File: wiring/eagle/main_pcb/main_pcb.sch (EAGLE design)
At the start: 19 parts

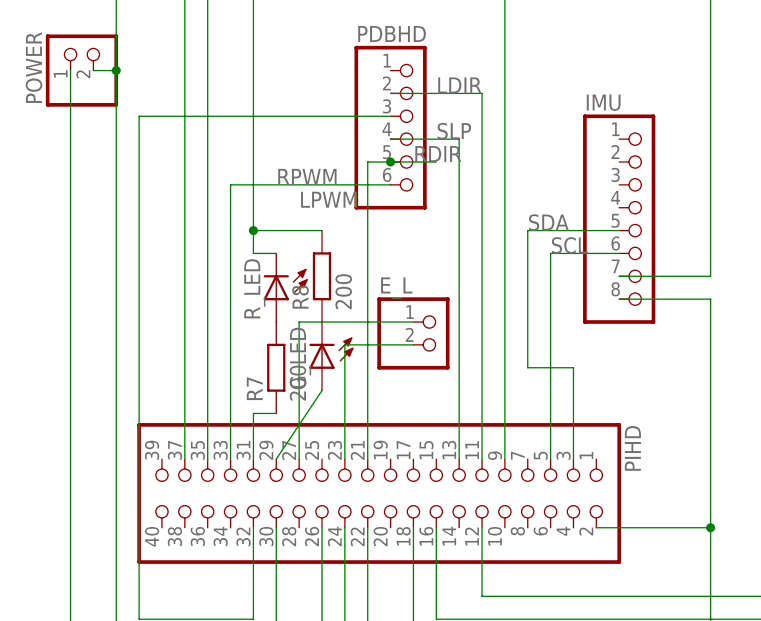
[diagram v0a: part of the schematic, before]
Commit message: Encoders, roomba, PID (#29)
* Started drive control software node, need to integrate with ros and write encoder reading software

* changed us data type

* Change package structure

* Fix typo in deploy.sh

* Added Roomba control node. This mostly works, but crues/motors.py does nothing, for reasons totally beyond us.

* The rooba roombas!

* Add roomba script which does the samething without involving ROS.

* Refactor ultrasonic module, and add code for getting scan of all three ranges

* Add timeout to get_range() - cf. #13

* Move GPIO configuration to a dedicated function, so that it is run only once.

* Handle UltrasonicTimeout in ROS node.

* Increased ultrasonic timeout based on HC-SR04 datasheet.

* Update deploy script paths

* Move launch file - 'robot' is already a ROS package, apparently.

* Better logging

* Change pin definitions to ones used on PCB (may need to be double checked)

* Add an LED module.

Only problem is interrupting flashing LED relies on Event stored in state, so any ROS nodes calling this must be using the same Python process. I think.

* Support multiple ultrasonic sensors.

* Better roomba node

* Add ROS LED node and make roomba turn lights on and off.

* Add eagle files

* Add PDFs

* Load pin numbers from JSON config file.

* Fixed a few issues with the roomba code. Still doesn't work consistently.

* Increase insulation around spacer holes to 5mm

* Add IMU spacer and other minor adjustments

* Add files via upload

* Add IP address config file

* Make deploy script talk to you.

* Fix roomba code

* Fix LED node (swapped green and red LEDs - green is now on the outside)

* Add encoder node

* Make changes to PCB to avoid using pin 27

* Wrong pins in new config file

* Make encoder node parameterised

* Parameterise LEDs

* Separate out drive nodes and rename launch file to roomba.launch

* Use Twist message to communicate with differential-drive packag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
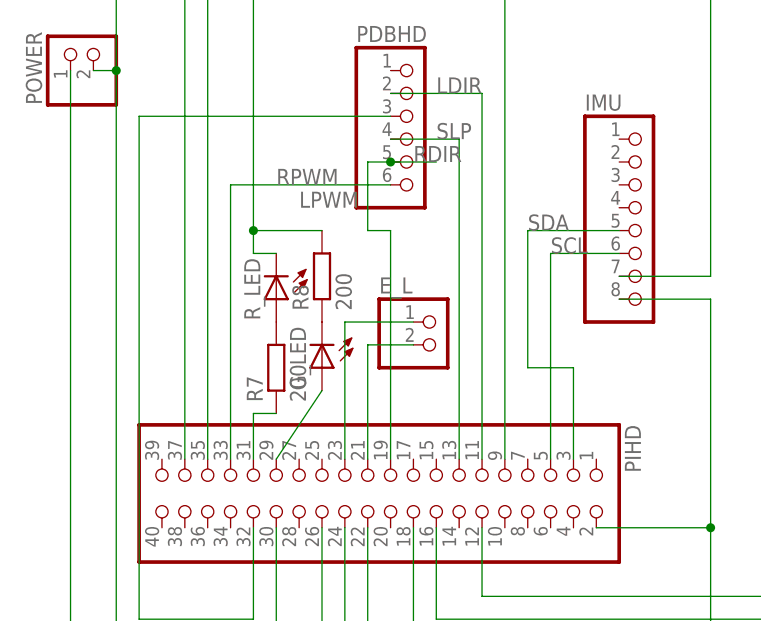
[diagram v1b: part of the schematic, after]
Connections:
- removed net EL_A: E_L.2, PIHD.23
- removed net EL_B: E_L.1, PIHD.27
- new net N$1: E_L.2, PIHD.21
- new net N$2: E_L.1, PIHD.23
- net RDIR: now also PIHD.19; no longer PIHD.21
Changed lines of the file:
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@@
 <?xml version="1.0" encoding="utf-8"?>
 <!DOCTYPE eagle SYSTEM "eagle.dtd">
-<eagle version="9.3.0">
+<eagle version="9.3.1">
 <drawing>
 <settings>
@@
 <label x="5.08" y="83.82" size="1.778" layer="95"/>
 <wire x1="2.54" y1="83.82" x2="7.62" y2="83.82" width="0.1524" layer="91"/>
-<pinref part="PIHD" gate="A" pin="21"/>
 <wire x1="2.54" y1="83.82" x2="0" y2="83.82" width="0.1524" layer="91"/>
-<wire x1="0" y1="83.82" x2="0" y2="50.8" width="0.1524" layer="91"/>
 <junction x="2.54" y="83.82"/>
+<pinref part="PIHD" gate="A" pin="19"/>
+<wire x1="2.54" y1="50.8" x2="2.54" y2="76.2" width="0.1524" layer="91"/>
+<wire x1="2.54" y1="76.2" x2="0" y2="76.2" width="0.1524" layer="91"/>
+<wire x1="0" y1="76.2" x2="0" y2="83.82" width="0.1524" layer="91"/>
 </segment>
 </net>
@@
 </segment>
 </net>
-<net name="EL_A" class="0">
-<segment>
-<pinref part="E_L" gate="G$1" pin="2"/>
-<pinref part="PIHD" gate="A" pin="23"/>
-<wire x1="5.08" y1="63.5" x2="-2.54" y2="63.5" width="0.1524" layer="91"/>
-<wire x1="-2.54" y1="63.5" x2="-2.54" y2="50.8" width="0.1524" layer="91"/>
-</segment>
-</net>
-<net name="EL_B" class="0">
-<segment>
-<pinref part="E_L" gate="G$1" pin="1"/>
-<pinref part="PIHD" gate="A" pin="27"/>
-<wire x1="5.08" y1="66.04" x2="-7.62" y2="66.04" width="0.1524" layer="91"/>
-<wire x1="-7.62" y1="66.04" x2="-7.62" y2="50.8" width="0.1524" layer="91"/>
-</segment>
-</net>
 <net name="ER_A" class="0">
 <segment>
@@
 </segment>
 </net>
+<net name="N$1" class="0">
+<segment>
+<pinref part="E_L" gate="G$1" pin="2"/>
+<pinref part="PIHD" gate="A" pin="21"/>
+<wire x1="5.08" y1="63.5" x2="0" y2="63.5" width="0.1524" layer="91"/>
+<wire x1="0" y1="63.5" x2="0" y2="50.8" width="0.1524" layer="91"/>
+</segment>
+</net>
+<net name="N$2" class="0">
+<segment>
+<pinref part="E_L" gate="G$1" pin="1"/>
+<pinref part="PIHD" gate="A" pin="23"/>
+<wire x1="5.08" y1="66.04" x2="-2.54" y2="66.04" width="0.1524" layer="91"/>
+<wire x1="-2.54" y1="66.04" x2="-2.54" y2="50.8" width="0.1524" layer="91"/>
+</segment>
+</net>
